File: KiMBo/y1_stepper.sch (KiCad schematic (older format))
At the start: 26 parts

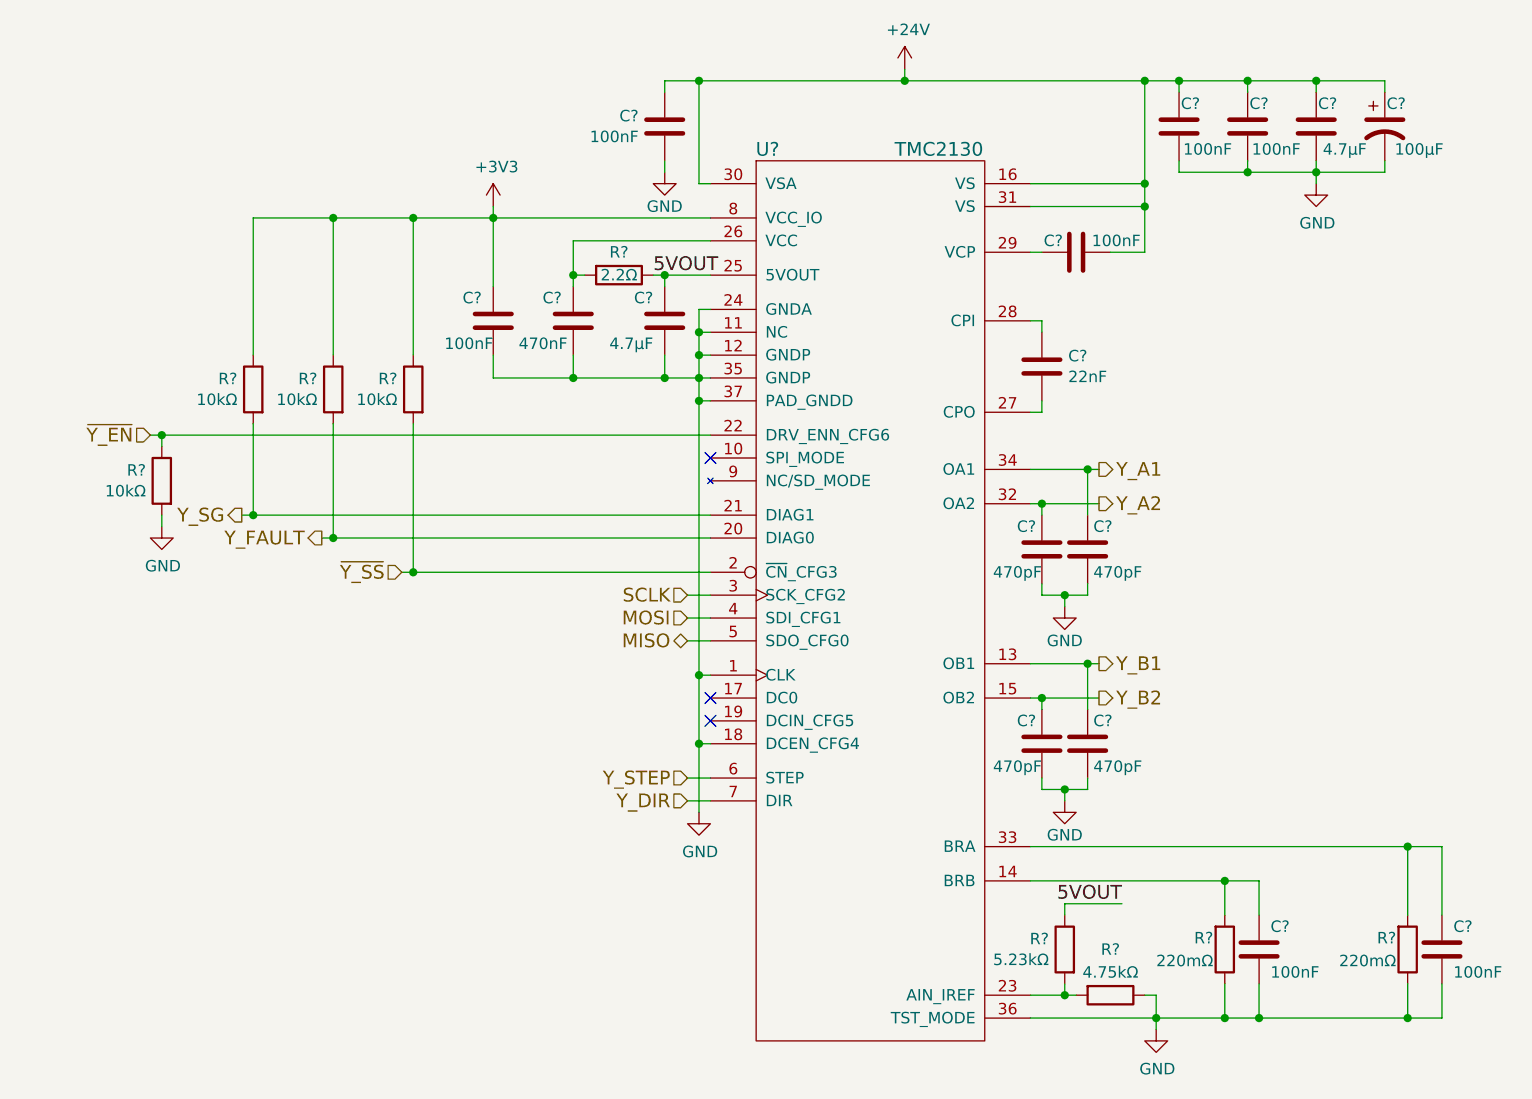
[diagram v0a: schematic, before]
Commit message: Update the rest of the power rails and add two more stepper drivers
Now has *nine* stepper drivers, this will increase cost, and may drastically increase development time...
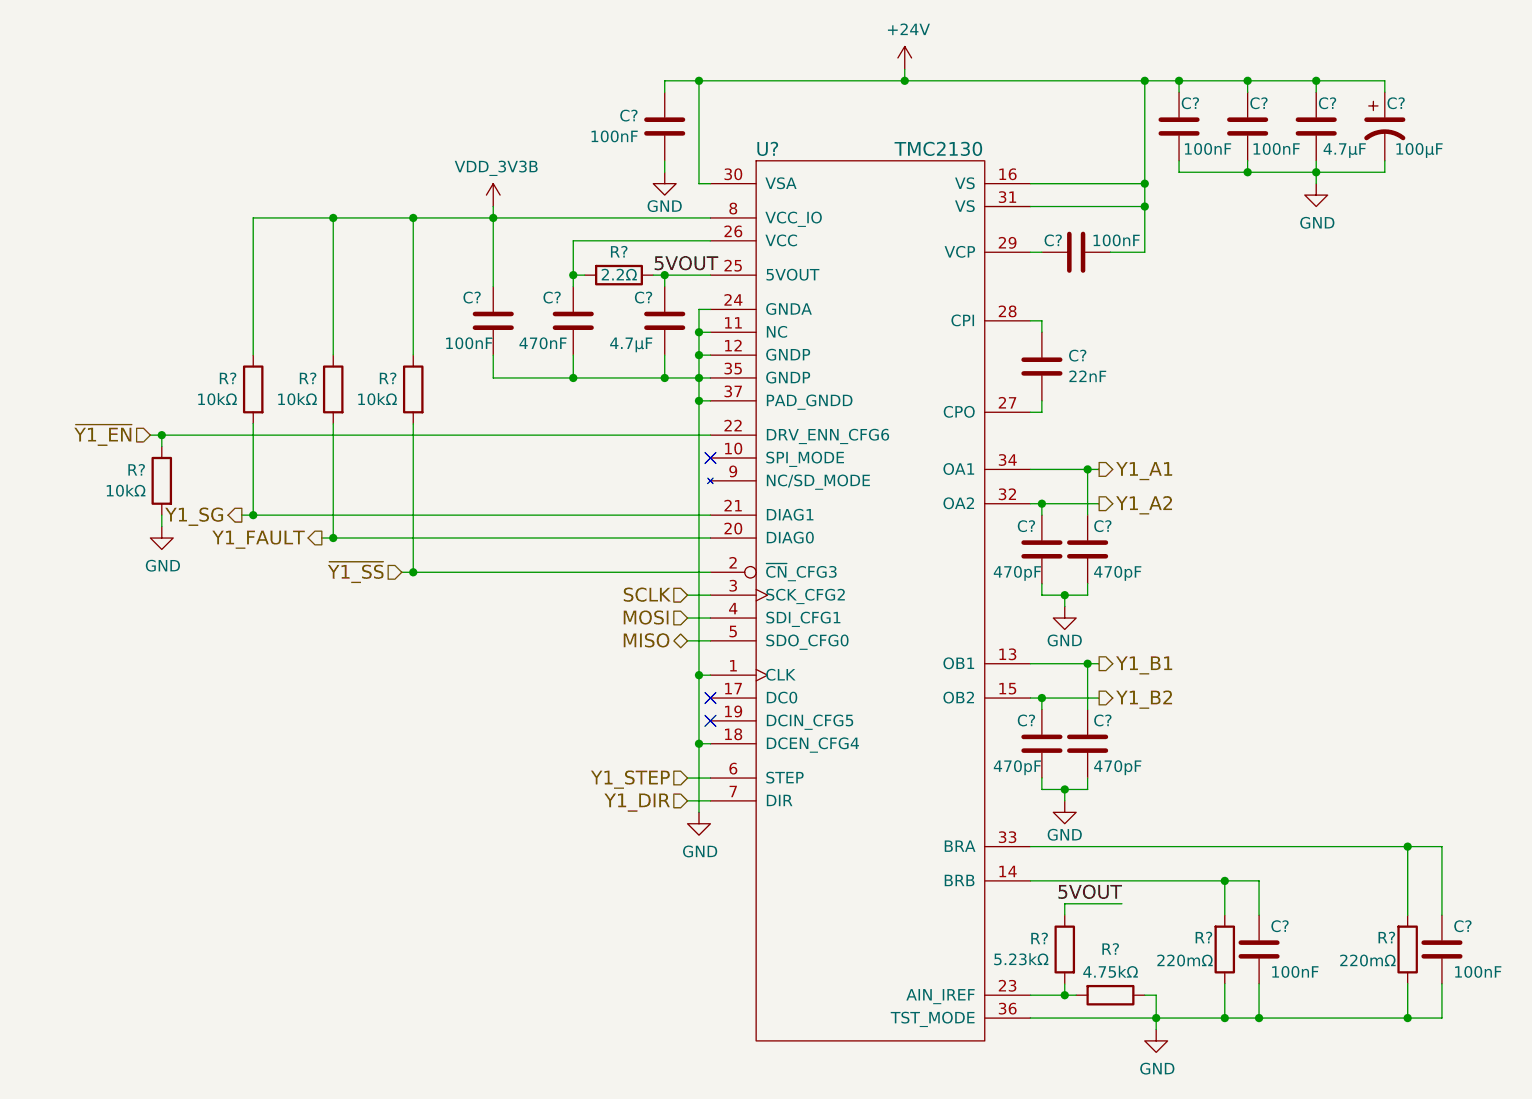
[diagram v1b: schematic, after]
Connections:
- net +3V3 renamed VDD_3V3B
- net Y_A1 renamed Y1_A1
- net Y_A2 renamed Y1_A2
- net Y_B1 renamed Y1_B1
- net Y_B2 renamed Y1_B2
- net Y_DIR renamed Y1_DIR
- net Y_FAULT renamed Y1_FAULT
- net Y_SG renamed Y1_SG
- net Y_STEP renamed Y1_STEP
- net ~Y_EN renamed ~Y1_EN
- net ~Y_SS renamed ~Y1_SS
